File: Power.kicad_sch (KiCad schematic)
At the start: 26 parts, among them Q1 SI2301BDS, U1 BATTERY, U2 TPS63070RNMR, U3 TPRT9013-33

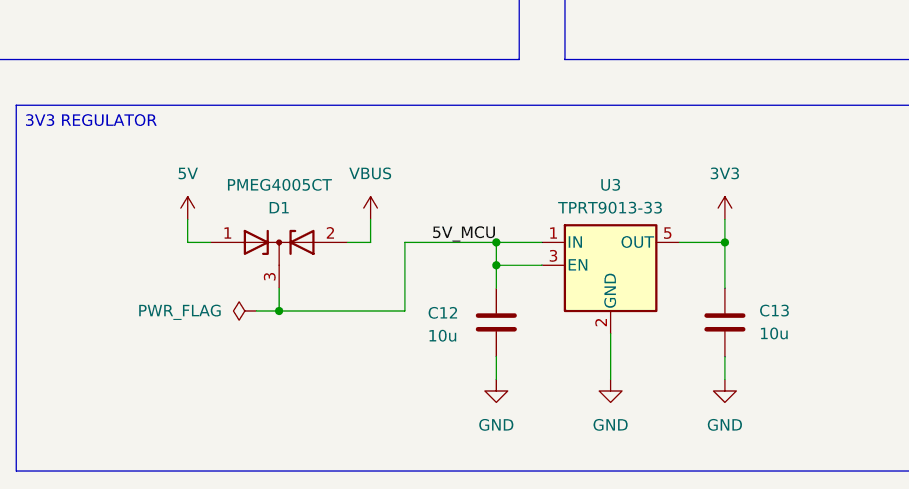
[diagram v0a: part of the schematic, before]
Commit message: Power layout and regulators
Changed the LDO regulators to TLV767.
Added missing power connections.

TODO:
Start the ELRS module layout.
Review previous iterations.
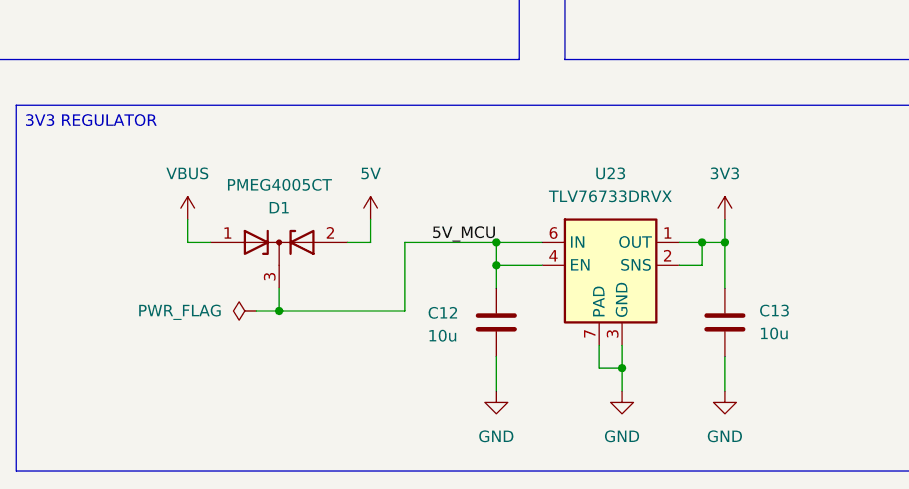
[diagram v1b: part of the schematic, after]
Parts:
- removed U3: TPRT9013-33, Package_TO_SOT_SMD:SOT-23-5, symbol Regulator_Linear:TLV70233_SOT23-5
- added U23: TLV76733DRVX, Package_SON:WSON-6-1EP_2x2mm_P0.65mm_EP1x1.6mm_ThermalVias, symbol Custom_Parts:TLV76733DRVX
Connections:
- net 3V3: now also U23.1 (OUT), U23.2 (SNS)
- net 5V: now also D1.2 (A); no longer D1.1 (A)
- net 5V_MCU: now also U23.4 (EN), U23.6 (IN)
- net GND: now also U23.3 (GND), U23.5 (GND), U23.7 (PAD)
- net VBUS: now also D1.1 (A); no longer D1.2 (A)

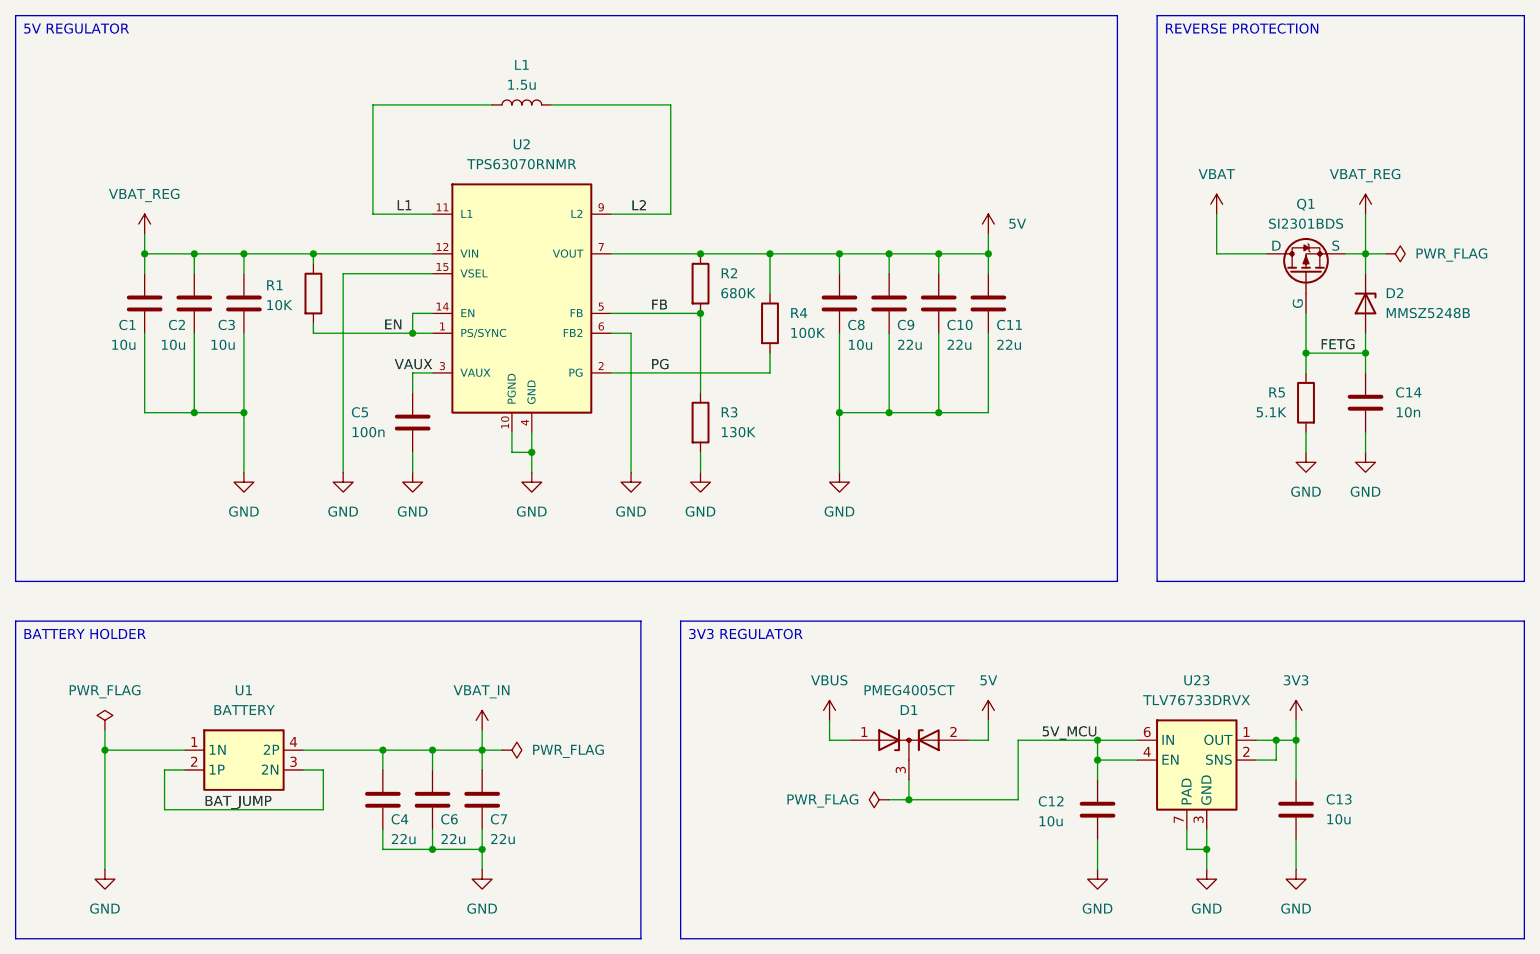
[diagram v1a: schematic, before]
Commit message: Voltage detection
Added a VBUS voltage detection for the RP.
Minor layout changes.
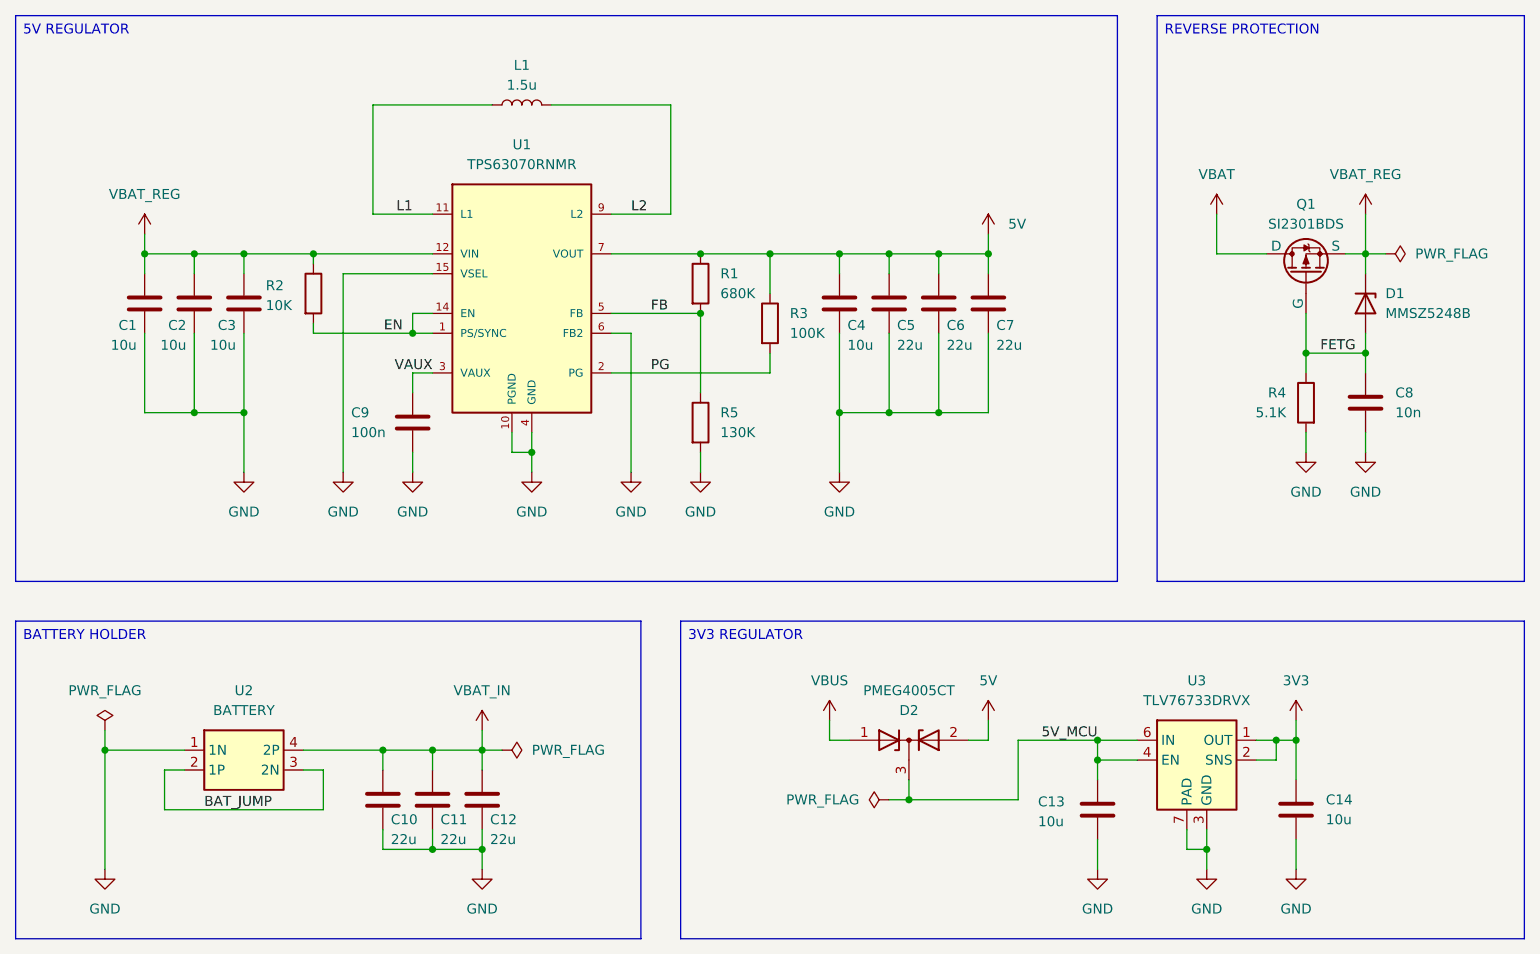
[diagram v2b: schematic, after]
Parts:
- renumbered C4 to C10, C6 to C11, C7 to C12, C12 to C13, C13 to C14, C8 to C4, C9 to C5, C10 to C6, C11 to C7, C14 to C8, C5 to C9, D2 to D1, D1 to D2, R2 to R1, R1 to R2, R4 to R3, R5 to R4, R3 to R5, U2 to U1, U1 to U2, U23 to U3
